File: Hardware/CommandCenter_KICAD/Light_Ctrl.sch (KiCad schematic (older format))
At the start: 49 parts

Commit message: Layout started
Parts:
- removed D?: LED, LEDs:LED_0603_HandSoldering, symbol Device:LED
- removed J?: SW0, NFC_Toy_Lib:Pad_SMD_Small, symbol Pad:Pad
- removed J?: SW1, NFC_Toy_Lib:Pad_SMD_Small, symbol Pad:Pad
- removed J?: SW2, NFC_Toy_Lib:Pad_SMD_Small, symbol Pad:Pad
- removed J?: SW3, NFC_Toy_Lib:Pad_SMD_Small, symbol Pad:Pad
- removed J?: SW0_RTN, NFC_Toy_Lib:Pad_SMD_Small, symbol Pad:Pad
- removed J?: SW1_RTN, NFC_Toy_Lib:Pad_SMD_Small, symbol Pad:Pad
- removed J?: SW2_RTN, NFC_Toy_Lib:Pad_SMD_Small, symbol Pad:Pad
- removed J?: SW3_RTN, NFC_Toy_Lib:Pad_SMD_Small, symbol Pad:Pad
- removed J?: LED0, NFC_Toy_Lib:Pad_SMD_Small, symbol Pad:Pad
- removed J?: LED0_RTN, NFC_Toy_Lib:Pad_SMD_Small, symbol Pad:Pad
- removed J?: LED1, NFC_Toy_Lib:Pad_SMD_Small, symbol Pad:Pad
- removed J?: LED1_RTN, NFC_Toy_Lib:Pad_SMD_Small, symbol Pad:Pad
- removed J?: LED2, NFC_Toy_Lib:Pad_SMD_Small, symbol Pad:Pad
- removed J?: LED2_RTN, NFC_Toy_Lib:Pad_SMD_Small, symbol Pad:Pad
- removed J?: LED3, NFC_Toy_Lib:Pad_SMD_Small, symbol Pad:Pad
- removed J?: LED3_RTN, NFC_Toy_Lib:Pad_SMD_Small, symbol Pad:Pad
- removed R?: 121, Resistors_SMD:R_0603_HandSoldering, symbol Device:R
- removed TP?: I2S_SD, symbol Connector:TestPoint
- added C23: 0.1u, Capacitor_SMD:C_0603_1608Metric_Pad1.05x0.95mm_HandSolder, symbol Device:C
- added J10: LED2, Connector_PinHeader_2.54mm:PinHeader_1x02_P2.54mm_Vertical, symbol Connector_Generic:Conn_01x02
- added J11: LED3, Connector_PinHeader_2.54mm:PinHeader_1x02_P2.54mm_Vertical, symbol Connector_Generic:Conn_01x02
- added J12: Wake, Connector_PinHeader_2.54mm:PinHeader_1x02_P2.54mm_Vertical, symbol Connector_Generic:Conn_01x02
- added J13: SW0, Connector_PinHeader_2.54mm:PinHeader_1x02_P2.54mm_Vertical, symbol Connector_Generic:Conn_01x02
- added J14: SW1, Connector_PinHeader_2.54mm:PinHeader_1x02_P2.54mm_Vertical, symbol Connector_Generic:Conn_01x02
- added J15: SW2, Connector_PinHeader_2.54mm:PinHeader_1x02_P2.54mm_Vertical, symbol Connector_Generic:Conn_01x02
- added J16: SW3, Connector_PinHeader_2.54mm:PinHeader_1x02_P2.54mm_Vertical, symbol Connector_Generic:Conn_01x02
- added J18: Bar Graph SW, Connector_PinHeader_2.54mm:PinHeader_1x09_P2.54mm_Vertical, symbol Connector_Generic:Conn_01x09
- added J8: LED0, Connector_PinHeader_2.54mm:PinHeader_1x02_P2.54mm_Vertical, symbol Connector_Generic:Conn_01x02
- added J9: LED1, Connector_PinHeader_2.54mm:PinHeader_1x02_P2.54mm_Vertical, symbol Connector_Generic:Conn_01x02
- added R32, R37, R38, R39, R41, R42, R43, R44, R46: 10k, Resistor_SMD:R_0603_1608Metric_Pad1.05x0.95mm_HandSolder, symbol Device:R
- added R40: 100k, Resistor_SMD:R_0603_1608Metric_Pad1.05x0.95mm_HandSolder, symbol Device:R
- added U7: APDS-9960, digikey-footprints:Ambient_Prox_APDS-9960, symbol dk_Optical-Sensors-Ambient-Light-IR-UV-Sensors:APDS-9960
- C18, C19, C20, C21, C22: renamed from C?; footprint Capacitors_SMD:C_0402 -> Capacitor_SMD:C_0603_1608Metric_Pad1.05x0.95mm_HandSolder
- D2: renamed from D?; footprint LEDs:LED_0603_HandSoldering -> LED_SMD:LED_0603_1608Metric_Pad1.05x0.95mm_HandSolder
- J17: renamed from J?; footprint Socket_Strips:Socket_Strip_Straight_2x05_Pitch2.54mm_SMD -> CommandCenter:JLink_Mini_0p05
- R19, R20, R21, R22, R23, R24, R25, R26, R27, R28, R29, R30, R31, R33, R34, R35, R36, R45: renamed from R?; footprint Resistors_SMD:R_0603_HandSoldering -> Resistor_SMD:R_0603_1608Metric_Pad1.05x0.95mm_HandSolder
- U6: renamed from U?; footprint NFC_Toy_Lib:QFP50P900X900X160-48N -> CommandCenter:QFP50P900X900X160-48N
- gave numbers to parts that had none: 4
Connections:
- net +3V3: now also R30.1, R31.1, R34.1, R35.1, C23.1, R32.1, R37.1, R38.1, R39.1, R40.1, R41.1, U7.5 (LEDA), U7.8 (VDD)
- net GND: now also C23.2, J12.2 (Pin_2), J13.2 (Pin_2), J14.2 (Pin_2), J15.2 (Pin_2), J16.2 (Pin_2), J18.9 (Pin_9), U7.6 (GND)
- net I2C_SCL: now also U7.7 (SCL)
- net I2C_SDA: now also U7.1 (SDA)
- net LED1: now also U6.12 (PA2); no longer U6.29 (PA8)
- net LED2: now also U6.29 (PA8); no longer U6.30 (PA9)
- net SWDIO_LIGHT: now also R40.2
- net WKUP: now also J12.1 (Pin_1), R32.2
- net BG_SPI_SS: now reaches U6.14 (PA4)
- net BG_SPI_SCK: now reaches U6.15 (PA5)
- net BG_SPI_MOSI: now reaches U6.17 (PA7)
- net BG_SW0: now reaches U6.20 (PB2)
- net BG_SW0: now also J18.1 (Pin_1), R37.2
- net at R35.2: now also U6.27 (PB14), J15.1 (Pin_1); no longer U6.21 (PB10)
- net at R36.2: now also U6.28 (PB15), J16.1 (Pin_1); no longer U6.22 (PB11)
- net at U6.25 (PB12): now also R33.2, J13.1 (Pin_1)
- net at U6.26 (PB13): now also R34.2, J14.1 (Pin_1)
- net AUDIO_UART_TX: now reaches U6.31 (PA10)
- net COLOR_INT: now reaches U6.38 (PA15)
- net COLOR_INT: now also U7.2 (INT)
- net BG_SW1: now reaches U6.39 (PB3)
- net BG_SW1: now also J18.2 (Pin_2), R38.2
- net BG_SW2: now reaches U6.40 (PB4)
- net BG_SW2: now also J18.3 (Pin_3), R39.2
- net BG_SW3: now reaches U6.41 (PB5)
- net BG_SW3: now also J18.4 (Pin_4), R41.2
- net BG_SW4: now reaches U6.45 (PB8)
- net BG_SW4: now also J18.5 (Pin_5), R42.2; no longer R33.2
- net BG_SW5: now reaches U6.46 (PB9)
- net BG_SW5: now also J18.6 (Pin_6), R43.2; no longer R34.2
- net at Q3.3 (D): now also J8.2 (Pin_2)
- net at R20.2: now also J8.1 (Pin_1)
- net at Q4.3 (D): now also J9.2 (Pin_2)
- net at R25.2: now also J9.1 (Pin_1)
- net at Q5.3 (D): now also J10.2 (Pin_2)
- net at R27.2: now also J10.1 (Pin_1)
- net at Q6.3 (D): now also J11.2 (Pin_2)
- net at R29.2: now also J11.1 (Pin_1)
- new net: U7.3 (LDR), U7.4 (LEDK)
- new net: R42.1, R43.1, R44.1, R46.1
- new net AUDIO_UART_RX: U6.30 (PA9)
- new net BG_SW6: J18.7 (Pin_7), R44.2, U6.21 (PB10)
- new net BG_SW7: J18.8 (Pin_8), R46.2, U6.22 (PB11)
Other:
- note added: "Bar Graph Switches"
- note added: "Color Sensor"
- note added: "LED Drivers"
- moved on the sheet: C18, C19, C20, C21, C22, D2, J17, Q3, Q4, Q5, Q6, R19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

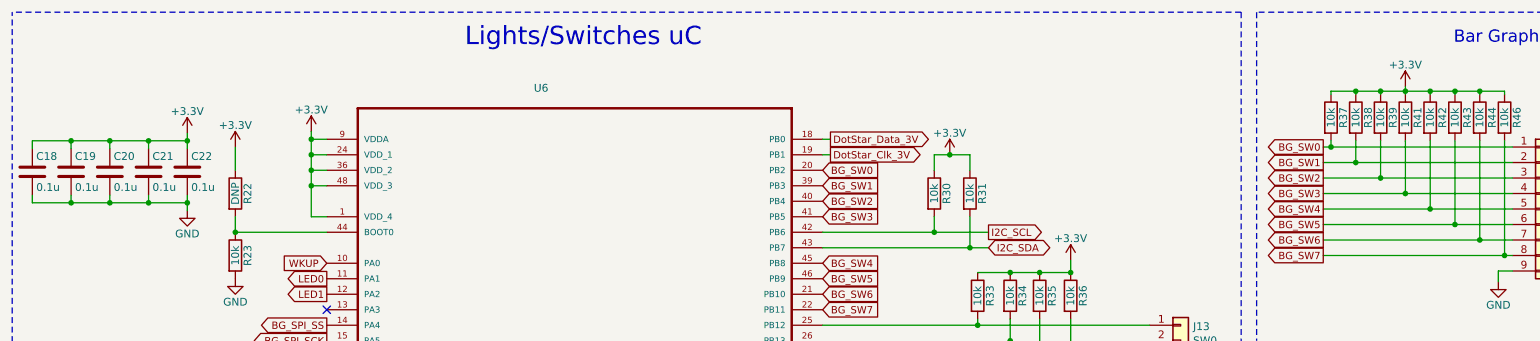
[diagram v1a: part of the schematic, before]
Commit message: Light Project Stable
DotStars and bar graph working. Getting master read nack on I2C to color sensor.
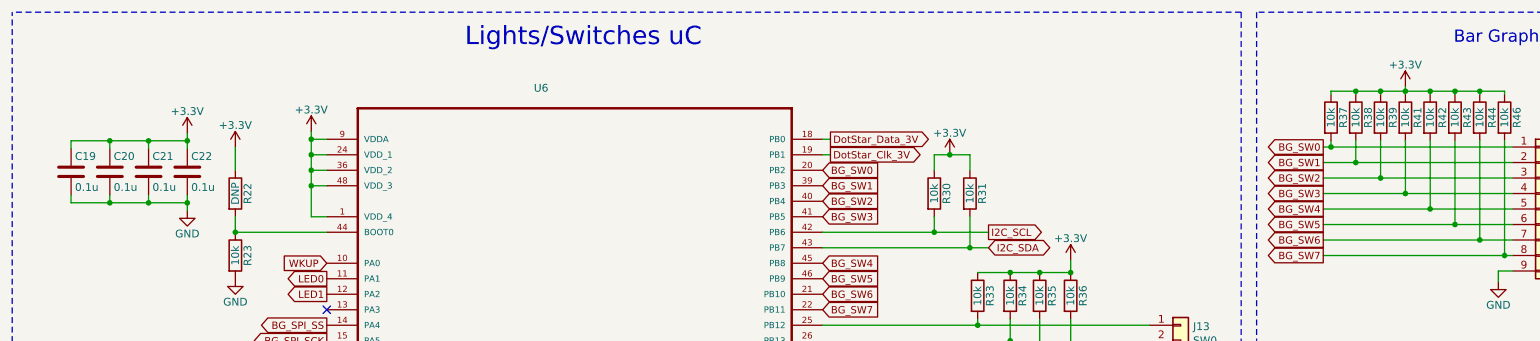
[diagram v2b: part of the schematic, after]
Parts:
- removed C18: 0.1u, Capacitor_SMD:C_0603_1608Metric_Pad1.05x0.95mm_HandSolder, symbol Device:C
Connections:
- net +3V3: now also R42.1, R43.1, R44.1, R46.1
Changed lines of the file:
@@
-$EndComp
-$Comp
-L Device:C C?
-U 1 1 5CF7406D
-P 700 1580
-AR Path="/5CF7406D" Ref="C?"  Part="1"
-AR Path="/5CF2E53C/5CF7406D" Ref="C18"  Part="1"
-F 0 "C18" H 725 1680 50  0000 L CNN
-F 1 "0.1u" H 725 1480 50  0000 L CNN
-F 2 "Capacitor_SMD:C_0603_1608Metric_Pad1.05x0.95mm_HandSolder" H 738 1430 50  0001 C CNN
-F 3 "" H 700 1580 50  0001 C CNN
-	1    700  1580
-	1    0    0    -1
 $EndComp
 $Comp
@@
 	1700 1780 1700 1830
 Wire Wire Line
-	700  1730 700  1780
-Wire Wire Line
-	700  1780 950  1780
-Wire Wire Line
 	950  1780 1200 1780
 Wire Wire Line
@@
 Connection ~ 1700 1780
 Wire Wire Line
-	700  1430 700  1380
-Wire Wire Line
-	700  1380 950  1380
-Wire Wire Line
 	950  1380 1200 1380
 Wire Wire Line
@@
 Wire Wire Line
 	950  1430 950  1380
-Connection ~ 950  1380
 Wire Wire Line
 	950  1730 950  1780
-Connection ~ 950  1780
 Wire Wire Line
 	1200 1730 1200 1780
@@
 $EndComp
 Wire Wire Line
-	9560 1030 9560 1060
-Wire Wire Line
 	9400 1080 9400 1060
 Wire Wire Line
 	9400 1060 9560 1060
-Connection ~ 9560 1060
-Wire Wire Line
-	9560 1060 9560 1080
 Wire Wire Line
 	9400 1060 9240 1060
@@
 	9720 1080 9720 1060
 Wire Wire Line
-	9720 1060 9570 1060
-Wire Wire Line
 	9720 1060 9880 1060
 Wire Wire Line
 	10200 1060 10200 1080
-Connection ~ 9720 1060
 Wire Wire Line
 	9880 1080 9880 1060
@@
 Wire Wire Line
 	5700 6830 5700 6890
+Wire Wire Line
+	9560 1030 9560 1060
+Wire Wire Line
+	9560 1060 9720 1060
+Connection ~ 9560 1060
+Wire Wire Line
+	9560 1060 9560 1080
+Connection ~ 9720 1060
 $EndSCHEMATC
